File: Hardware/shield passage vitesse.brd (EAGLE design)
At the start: 69.2 x 53.4 mm, 37 parts, among them Q1 2N7000, Q2 2N7000, Q3 2N7000, Q4 2N7000, Q5 2N7000

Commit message: Passage de la Zener à 14V
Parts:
- D1: value ZENER 15V -> ZENER 14V
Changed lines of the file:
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@@
 <attribute name="VALUE" x="22.733" y="14.351" size="1.27" layer="27" ratio="10"/>
 </element>
-<element name="D1" library="diode" package="DO41Z10" value="ZENER 15V" x="25.146" y="3.048" smashed="yes">
+<element name="D1" library="diode" package="DO41Z10" value="ZENER 14V" x="25.146" y="3.048" smashed="yes">
 <attribute name="VALUE" x="20.701" y="0.254" size="1.27" layer="27" ratio="10"/>
 </element>
@@
 <wire x1="51.181" y1="48.26" x2="45.72" y2="48.26" width="0.6096" layer="16"/>
 <wire x1="45.72" y1="48.26" x2="35.56" y2="38.1" width="0.6096" layer="16"/>
-<wire x1="35.56" y1="13.97" x2="35.56" y2="38.1" width="0.6096" layer="16"/>
-<wire x1="41.275" y1="10.033" x2="38.1" y2="10.033" width="0.6096" layer="16"/>
-<wire x1="38.1" y1="10.033" x2="36.83" y2="11.303" width="0.6096" layer="16"/>
-<wire x1="36.83" y1="11.303" x2="36.83" y2="12.7" width="0.6096" layer="16"/>
-<wire x1="36.83" y1="12.7" x2="35.56" y2="13.97" width="0.6096" layer="16"/>
+<wire x1="35.56" y1="11.7475" x2="35.56" y2="38.1" width="0.6096" layer="16"/>
+<wire x1="41.275" y1="10.033" x2="37.2745" y2="10.033" width="0.6096" layer="16"/>
+<wire x1="37.2745" y1="10.033" x2="35.56" y2="11.7475" width="0.6096" layer="16"/>
 </signal>
 <signal name="OUT4_12V">

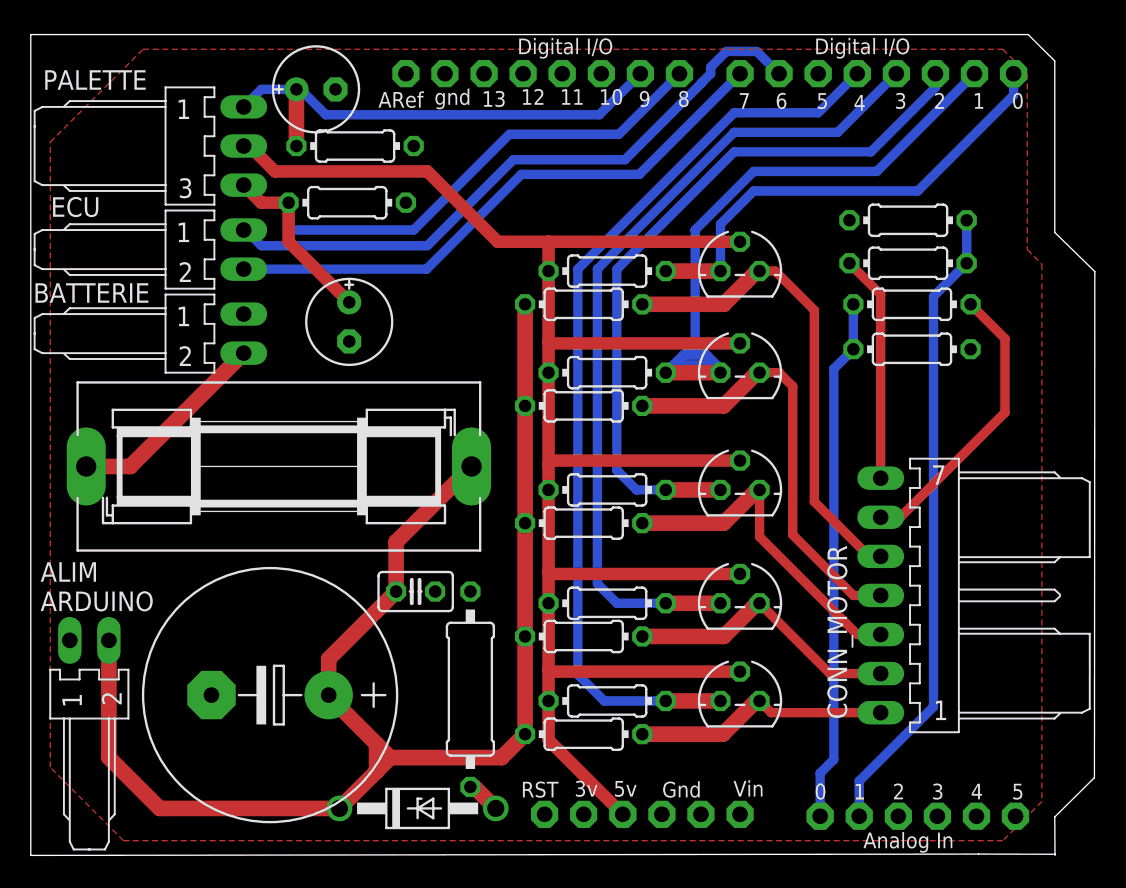
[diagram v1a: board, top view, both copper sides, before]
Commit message: Création de fichiers d'usinage
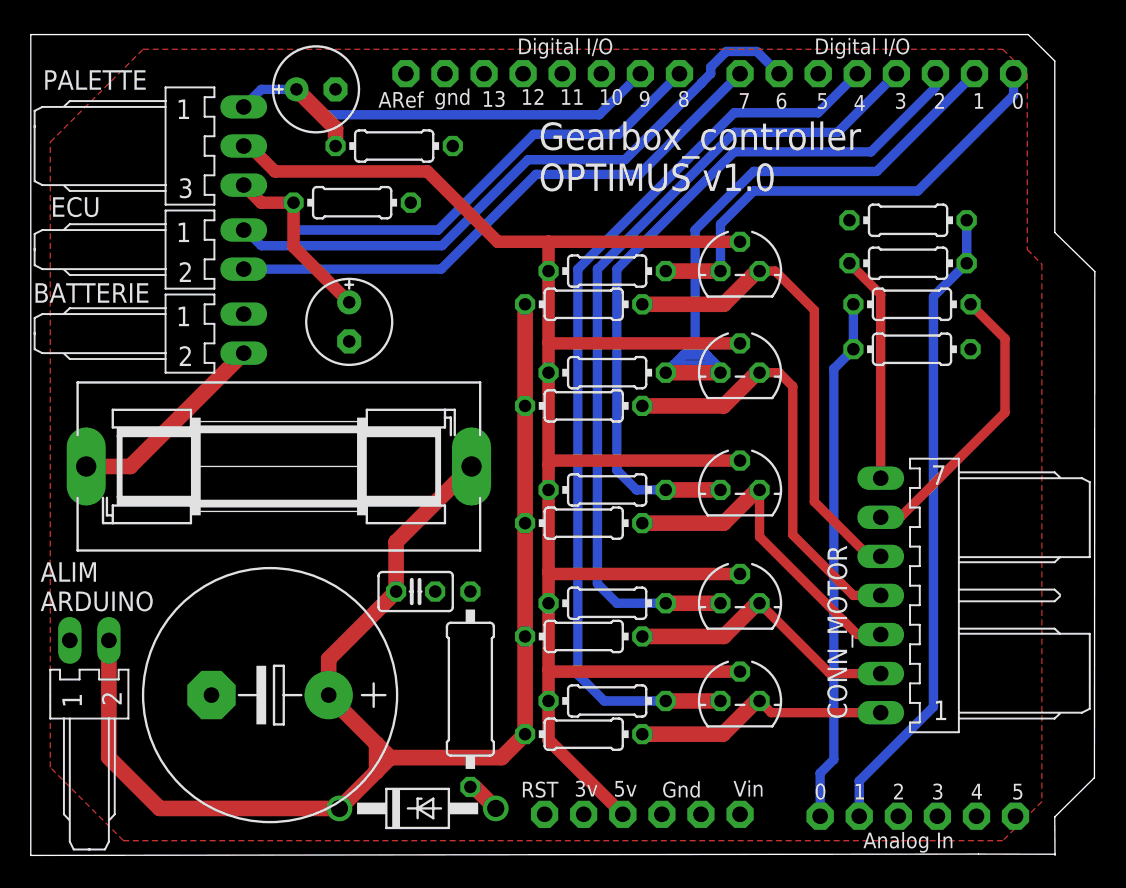
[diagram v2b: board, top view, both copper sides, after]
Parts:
- moved R15 2.54 mm to (23.6, 46.1)
- moved R17 0.32 mm to (20.9, 42.4)
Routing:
- net PALETTE_GAUCHE: track 31.7 -> 32.8 mm
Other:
- board text added: "Gearbox_controller OPTIMUS v1.0"
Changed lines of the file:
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@@
 <text x="0.635" y="15.875" size="1.27" layer="25">ALIM
 ARDUINO</text>
+<text x="33.02" y="43.18" size="1.778" layer="25">Gearbox_controller
+OPTIMUS v1.0</text>
 </plain>
 <attributes>
@@
 </element>
 <element name="C4" library="rcl" package="E2,5-6E" value="0.33µF" x="18.542" y="49.784" smashed="yes">
-<attribute name="VALUE" x="10.414" y="50.419" size="1.27" layer="27" ratio="10"/>
-</element>
-<element name="R17" library="resistor" package="0204/7" value="10k" x="20.574" y="42.418" smashed="yes">
-<attribute name="VALUE" x="18.9484" y="41.9354" size="0.9906" layer="27" ratio="10"/>
+<attribute name="VALUE" x="10.0965" y="50.419" size="1.27" layer="27" ratio="10"/>
+</element>
+<element name="R17" library="resistor" package="0204/7" value="10k" x="20.8915" y="42.418" smashed="yes">
+<attribute name="VALUE" x="19.2659" y="41.9354" size="0.9906" layer="27" ratio="10"/>
 </element>
 <element name="C5" library="rcl" package="E2,5-6E" value="0.33µF" x="20.701" y="34.671" smashed="yes" rot="R270">
@@
 <attribute name="VALUE" x="27.8892" y="12.065" size="1.27" layer="27" ratio="10" rot="R270"/>
 </element>
-<element name="R15" library="resistor" package="0204/7" value="10k" x="21.082" y="46.101" smashed="yes">
-<attribute name="VALUE" x="19.4564" y="45.6184" size="0.9906" layer="27" ratio="10"/>
+<element name="R15" library="resistor" package="0204/7" value="10k" x="23.622" y="46.101" smashed="yes">
+<attribute name="VALUE" x="21.9964" y="45.6184" size="0.9906" layer="27" ratio="10"/>
 </element>
 <element name="CONN_MOTOR" library="EP_molex_6410_7395" package="7395-07" value="22-05-7078-07" x="55.245" y="16.891" smashed="yes" rot="R270">
@@
 <wire x1="39.624" y1="50.8" x2="36.957" y2="48.133" width="0.6096" layer="16"/>
 <wire x1="36.957" y1="48.133" x2="19.176990625" y2="48.133" width="0.6096" layer="16"/>
-<wire x1="17.272" y1="46.101" x2="17.272" y2="49.784" width="1.016" layer="1"/>
+<wire x1="19.812" y1="47.244" x2="17.272" y2="49.784" width="1.016" layer="1"/>
+<wire x1="19.812" y1="47.244" x2="19.812" y2="46.101" width="1.016" layer="1"/>
 <wire x1="19.176990625" y1="48.133" x2="17.525990625" y2="49.784" width="0.6096" layer="16"/>
 <wire x1="17.525990625" y1="49.784" x2="17.272" y2="49.784" width="0.6096" layer="16"/>
@@
 <contactref element="DIGITALIN8_13" pad="8"/>
 <wire x1="42.164" y1="50.8" x2="38.227" y2="46.863" width="0.6096" layer="16"/>
-<wire x1="31.115" y1="46.863" x2="38.227" y2="46.863" width="0.6096" layer="16"/>
-<wire x1="16.764" y1="42.418" x2="16.764" y2="40.894" width="0.6096" layer="16"/>
-<wire x1="16.764" y1="40.894" x2="17.018" y2="40.64" width="0.6096" layer="16"/>
-<wire x1="24.892" y1="40.64" x2="31.115" y2="46.863" width="0.6096" layer="16"/>
-<wire x1="17.018" y1="40.64" x2="24.892" y2="40.64" width="0.6096" layer="16"/>
+<wire x1="32.7025" y1="46.863" x2="38.227" y2="46.863" width="0.6096" layer="16"/>
+<wire x1="17.0815" y1="42.418" x2="17.0815" y2="40.64" width="0.6096" layer="16"/>
+<wire x1="26.4795" y1="40.64" x2="32.7025" y2="46.863" width="0.6096" layer="16"/>
+<wire x1="17.0815" y1="40.64" x2="26.4795" y2="40.64" width="0.6096" layer="16"/>
 <wire x1="13.843" y1="43.561" x2="14.986" y2="42.418" width="0.8128" layer="1"/>
-<wire x1="14.986" y1="42.418" x2="16.764" y2="42.418" width="0.8128" layer="1"/>
-<wire x1="16.764" y1="42.418" x2="16.764" y2="39.878" width="0.8128" layer="1"/>
-<wire x1="16.764" y1="39.878" x2="20.701" y2="35.941" width="0.8128" layer="1"/>
+<wire x1="14.986" y1="42.418" x2="17.0815" y2="42.418" width="0.8128" layer="1"/>
+<wire x1="17.0815" y1="42.418" x2="17.0815" y2="39.5605" width="0.8128" layer="1"/>
+<wire x1="17.0815" y1="39.5605" x2="20.701" y2="35.941" width="0.8128" layer="1"/>
 </signal>
 <signal name="SHIFT_CUT">
@@
 <contactref element="DIGITALIN0_7" pad="8"/>
 <wire x1="46.101" y1="50.8" x2="39.5605" y2="44.2595" width="0.6096" layer="16"/>
-<wire x1="39.5605" y1="44.2595" x2="31.8897" y2="44.2595" width="0.6096" layer="16"/>
-<wire x1="25.7302" y1="38.1" x2="13.843" y2="38.1" width="0.6096" layer="16"/>
-<wire x1="31.8897" y1="44.2595" x2="25.7302" y2="38.1" width="0.6096" layer="16"/>
+<wire x1="39.5605" y1="44.2595" x2="32.8422" y2="44.2595" width="0.6096" layer="16"/>
+<wire x1="26.6827" y1="38.1" x2="13.843" y2="38.1" width="0.6096" layer="16"/>
+<wire x1="32.8422" y1="44.2595" x2="26.6827" y2="38.1" width="0.6096" layer="16"/>
 </signal>
 <signal name="SHIFT_POT">
@@
 <wire x1="44.196" y1="50.8" x2="44.196" y2="51.2318" width="0.6096" layer="16"/>
 <wire x1="43.6118" y1="50.2158" x2="44.196" y2="50.8" width="0.6096" layer="16"/>
-<wire x1="31.369" y1="45.212" x2="25.781" y2="39.624" width="0.6096" layer="16"/>
-<wire x1="38.6235" y1="45.212" x2="31.369" y2="45.212" width="0.6096" layer="16"/>
-<wire x1="25.781" y1="39.624" x2="14.986" y2="39.624" width="0.6096" layer="16"/>
+<wire x1="32.3215" y1="45.212" x2="26.7335" y2="39.624" width="0.6096" layer="16"/>
+<wire x1="38.6235" y1="45.212" x2="32.3215" y2="45.212" width="0.6096" layer="16"/>
+<wire x1="26.7335" y1="39.624" x2="14.986" y2="39.624" width="0.6096" layer="16"/>
 <wire x1="14.986" y1="39.624" x2="13.97" y2="40.64" width="0.6096" layer="16"/>
 <wire x1="13.97" y1="40.64" x2="13.843" y2="40.64" width="0.6096" layer="16"/>
@@
 <contactref element="C2" pad="1"/>
 <contactref element="D1" pad="C"/>
-<wire x1="28.829" y1="25.0952" x2="28.6512" y2="25.273" width="1.016" layer="1"/>
 <wire x1="28.6512" y1="25.273" x2="23.749" y2="20.3708" width="1.016" layer="1"/>
 <wire x1="23.749" y1="20.3708" x2="23.749" y2="17.145" width="1.016" layer="1"/>
